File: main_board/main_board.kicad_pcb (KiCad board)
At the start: 2 copper layers, 20.3 x 15.2 mm, 18 parts, among them J1 Conn_01x03, J2 Conn_01x03, U1 STC15W201S-35x-SOP16, U2 AP130-15Y

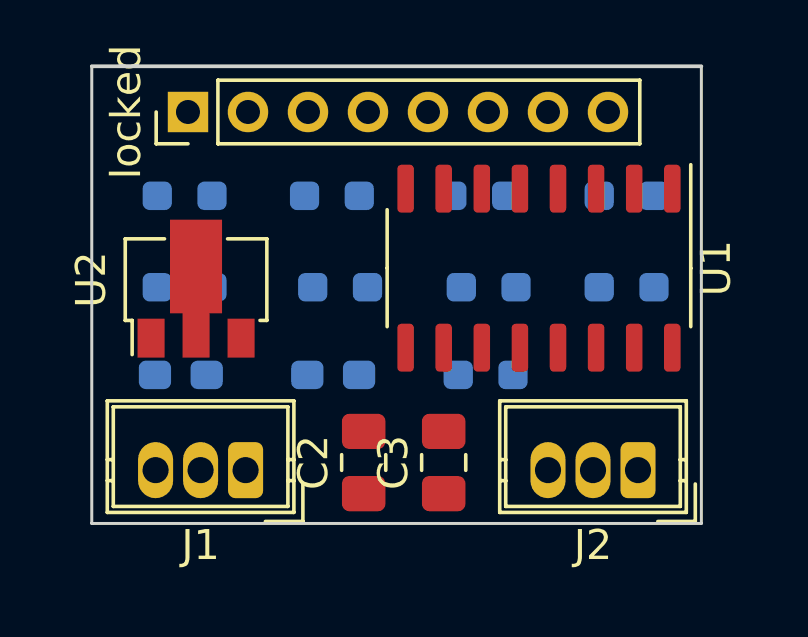
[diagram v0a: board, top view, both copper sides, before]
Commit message: feat(main_board): connect net
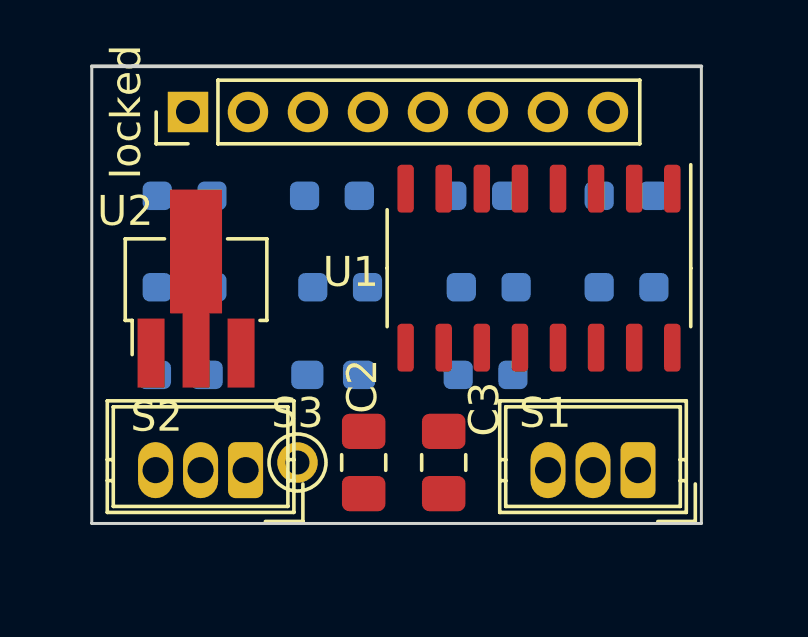
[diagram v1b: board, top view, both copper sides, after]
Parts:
- removed J1, J2: Conn_01x03, Connector_Wuerth:Wuerth_WR-WTB_64800311622_1x03_P1.50mm_Vertical
- added S1: Conn_01x03, Connector_Wuerth:Wuerth_WR-WTB_64800311622_1x03_P1.50mm_Vertical, F.Cu at (145.2, 89.7)
- added S2: Conn_01x03, Connector_Wuerth:Wuerth_WR-WTB_64800311622_1x03_P1.50mm_Vertical, F.Cu at (132.1, 89.7)
- added S3: Conn_01x01, TestPoint:TestPoint_THTPad_D1.5mm_Drill0.7mm, F.Cu at (133.9, 89.4)
- U2: value AP130-15Y -> AMS1117-5.0; footprint Package_TO_SOT_SMD:SOT-89-3 -> Package_TO_SOT_SMD:SOT-89-3_Handsoldering
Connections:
- C1 pad 1: (no net) -> +5V
- C1 pad 2: (no net) -> GND
- C2 pad 1: (no net) -> +5V
- C2 pad 2: (no net) -> GND
- C3 pad 1: (no net) -> /VCC
- C3 pad 2: (no net) -> GND
- C4 pad 1: (no net) -> /VCC
- C4 pad 2: (no net) -> GND
- R1 pad 1: (no net) -> /P1.4
- R1 pad 2: (no net) -> /HL
- R2 pad 1: (no net) -> /P3.2
- R2 pad 2: (no net) -> /R
- R3 pad 1: (no net) -> /P3.1
- R3 pad 2: (no net) -> /F
- R4 pad 1: (no net) -> /P3.0
- R4 pad 2: (no net) -> /TL
- R5 pad 1: (no net) -> /P3.6
- R5 pad 2: (no net) -> /TL
- R6 pad 1: (no net) -> /P1.5
- R6 pad 2: (no net) -> /HL
- R7 pad 1: (no net) -> /P1.3
- R7 pad 2: (no net) -> /RT
- R8 pad 1: (no net) -> /P1.2
- R8 pad 2: (no net) -> /LT
- R9 pad 1: (no net) -> /P3.6
- R9 pad 2: (no net) -> /FW
- U1 pad 1: (no net) -> /P1.2
- U1 pad 10: (no net) -> /P3.1
- U1 pad 11: (no net) -> /P3.2
- U1 pad 12: (no net) -> unconnected-(U1-INT1/P3.3-Pad12)
- U1 pad 13: (no net) -> /P3.6
- U1 pad 14: (no net) -> /P3.7
- U1 pad 15: (no net) -> /P1.0
- U1 pad 16: (no net) -> /P1.1
- U1 pad 2: (no net) -> /P1.3
- U1 pad 3: (no net) -> /P1.4
- U1 pad 4: (no net) -> /P1.5
- U1 pad 5: (no net) -> unconnected-(U1-CMP-/MCLKO/RST/P5.4-Pad5)
- U1 pad 6: (no net) -> /VCC
- U1 pad 7: (no net) -> unconnected-(U1-CMP+/P5.5-Pad7)
- U1 pad 8: (no net) -> GND
- U1 pad 9: (no net) -> /P3.0
- U2 pad 1: (no net) -> GND
- U2 pad 2: (no net) -> /VCC
- U2 pad 3: (no net) -> +5V
- locked pad 1: (no net) -> /VCC
- locked pad 2: (no net) -> /HL
- locked pad 3: (no net) -> /FW
- locked pad 4: (no net) -> /TL
- locked pad 5: (no net) -> /F
- locked pad 6: (no net) -> /R
- locked pad 7: (no net) -> /RT
- locked pad 8: (no net) -> /LT

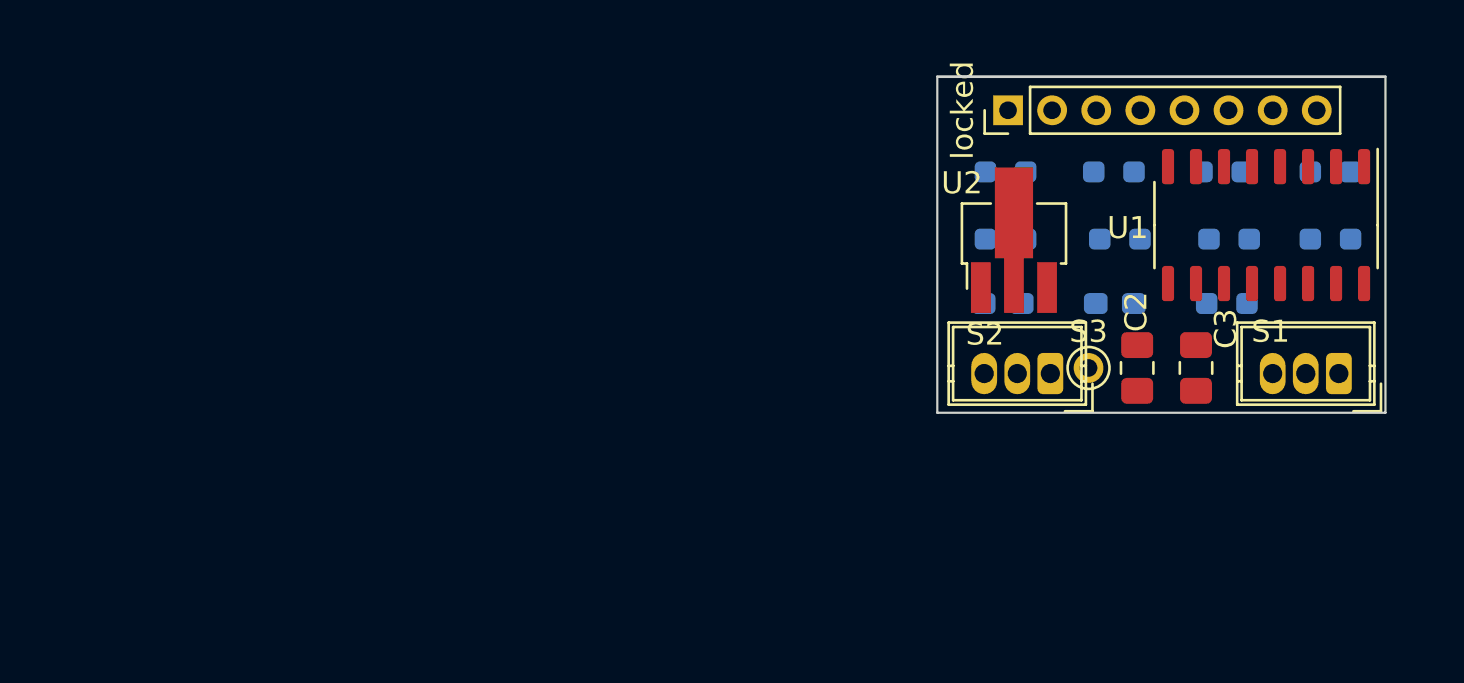
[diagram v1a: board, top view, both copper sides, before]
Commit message: feat(board/mcu): change mcu to sn32f805
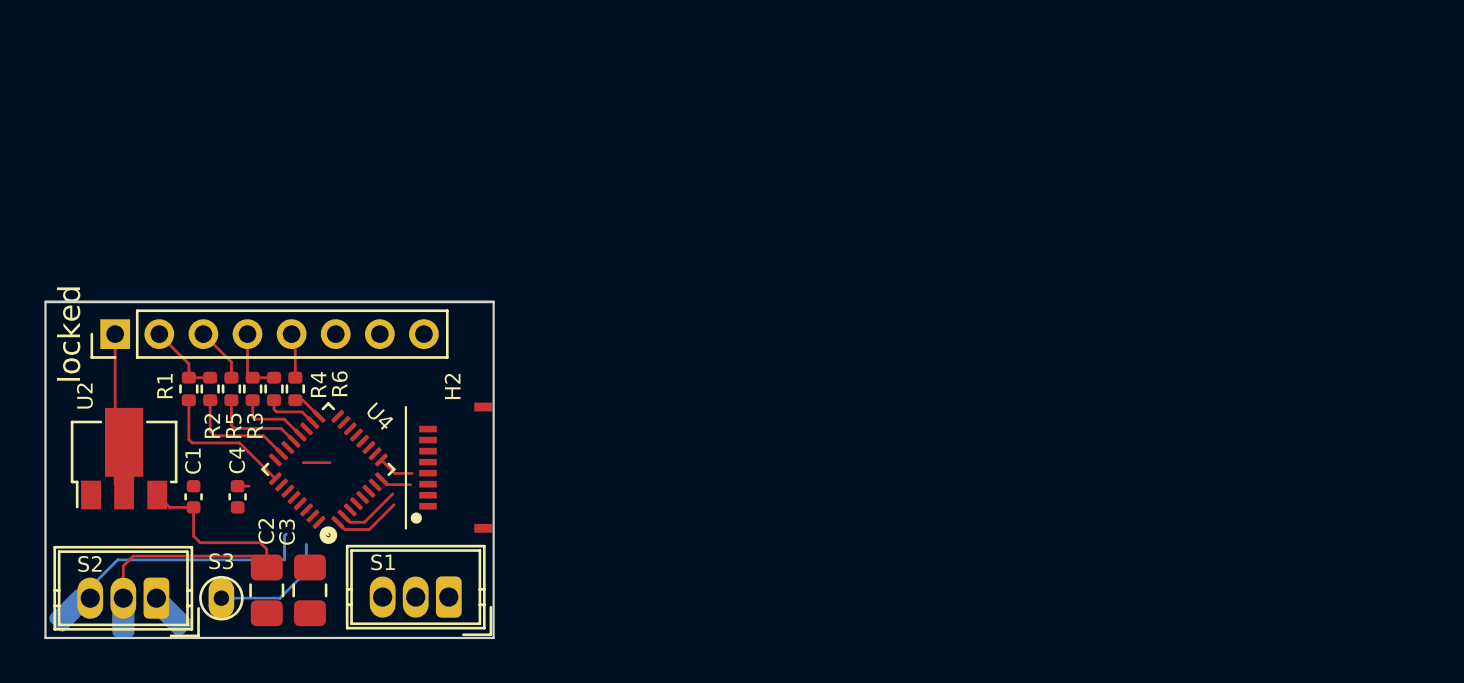
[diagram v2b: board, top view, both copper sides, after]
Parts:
- removed R7, R8, R9: R, Resistor_SMD:R_0603_1608Metric_Pad0.98x0.95mm_HandSolder
- removed U1: STC15W201S-35x-SOP16, Package_SO:STC_SOP-16_3.9x9.9mm_P1.27mm
- added H2: Conn_01x08, Connector_FFC-FPC:TE_0-1734839-8_1x08-1MP_P0.5mm_Horizontal, F.Cu at (104.8, 93.9)
- added REF**: SolderWirePad_1x01_SMD_1x2mm, Connector_Wire:SolderWirePad_1x01_SMD_1x2mm, B.Cu at (92.3, 100.6)
- added REF**: SolderWirePad_1x01_SMD_1x2mm, Connector_Wire:SolderWirePad_1x01_SMD_1x2mm, B.Cu at (87.7, 100.4)
- added REF**: SolderWirePad_1x01_SMD_1x2mm, Connector_Wire:SolderWirePad_1x01_SMD_1x2mm, B.Cu at (90.1, 100.6)
- added U4: SN32F805J/F, Package_DFN_QFN:QFN-32-1EP_4x4mm_P0.4mm_EP2.9x2.9mm, F.Cu at (99.4, 94.0)
- C1, C4: footprint Capacitor_SMD:C_0603_1608Metric_Pad1.08x0.95mm_HandSolder -> Capacitor_SMD:C_0402_1005Metric; moved to F.Cu
- R1, R2, R3, R4, R5, R6: footprint Resistor_SMD:R_0603_1608Metric_Pad0.98x0.95mm_HandSolder -> Resistor_SMD:R_0402_1005Metric; moved to F.Cu
- U2: footprint Package_TO_SOT_SMD:SOT-89-3_Handsoldering -> Package_TO_SOT_SMD:SOT-89-3
- moved R1 52.2 mm to (93.1, 90.4), turned to 90 degrees
- moved R6 42.9 mm to (97.9, 90.4), turned to 90 degrees
- moved R2 41.8 mm to (94.0, 90.4), turned to 90 degrees
- moved S2 41.8 mm to (91.6, 99.8)
- moved locked 41.7 mm to (89.7, 87.9)
- moved S1 41.6 mm to (104.9, 99.8)
- moved U2 41.5 mm to (90.1, 93.2)
- moved C3 41.4 mm to (98.6, 99.5), turned to -90 degrees
- moved C2 40.7 mm to (96.6, 99.5), turned to -90 degrees
- moved C4 40.7 mm to (95.3, 95.2), turned to -90 degrees
- moved S3 40.7 mm to (94.5, 99.8)
- moved R4 39.3 mm to (96.9, 90.4), turned to 90 degrees
- moved C1 37.7 mm to (93.3, 95.2), turned to 90 degrees
- moved R5 36.5 mm to (95.0, 90.4), turned to 90 degrees
- moved R3 34.8 mm to (96.0, 90.4), turned to 90 degrees
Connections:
- R1 pad 1: /P1.4 -> /HEAD_0
- R1 pad 2: /HL -> /LED_HEAD
- R2 pad 1: /P3.2 -> /HEAD_1
- R2 pad 2: /R -> /LED_HEAD
- R3 pad 1: /P3.1 -> /TAIL_0
- R3 pad 2: /F -> /LED_TAIL
- R4 pad 1: /P3.0 -> /TAIL_1
- R4 pad 2: /TL -> /LED_TAIL
- R5 pad 1: /P3.6 -> /CHASSIS
- R5 pad 2: /TL -> /LED_CHASSIS
- R6 pad 1: /P1.5 -> /FIRE
- R6 pad 2: /HL -> /LED_FIRE
- S3 pad 1: /P3.7 -> unconnected-(S3-Pin_1-Pad1)
- locked pad 2: /HL -> /LED_HEAD
- locked pad 3: /FW -> /LED_CHASSIS
- locked pad 4: /TL -> /LED_TAIL
- locked pad 5: /F -> /LED_FIRE
- locked pad 6: /R -> unconnected-(JSL1-Pin_6-Pad6)
- locked pad 7: /RT -> unconnected-(JSL1-Pin_7-Pad7)
- locked pad 8: /LT -> unconnected-(JSL1-Pin_8-Pad8)
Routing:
- net +5V: track 0.00 -> 15.9 mm
- net /P1.0: track 0.00 -> 11.0 mm
- net /VCC: track 0.00 -> 7.90 mm
- net /HEAD_0: track 0.00 -> 6.45 mm
- net unconnected-(S3-Pin_1-Pad1): track 0.00 -> 5.59 mm
- net /HEAD_1: track 0.00 -> 4.80 mm
- net /CHASSIS: track 0.00 -> 4.28 mm
- net /LED_HEAD: track 0.00 -> 3.49 mm
- net /SWDIO: track 0.00 -> 3.15 mm
- net /LED_TAIL: track 0.00 -> 3.04 mm
- net /TAIL_0: track 0.00 -> 2.92 mm
- net /SWCLK: track 0.00 -> 2.86 mm
- net /LED_CHASSIS: track 0.00 -> 2.50 mm
- net /TAIL_1: track 0.00 -> 2.42 mm
- net /LED_FIRE: track 0.00 -> 2.05 mm
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
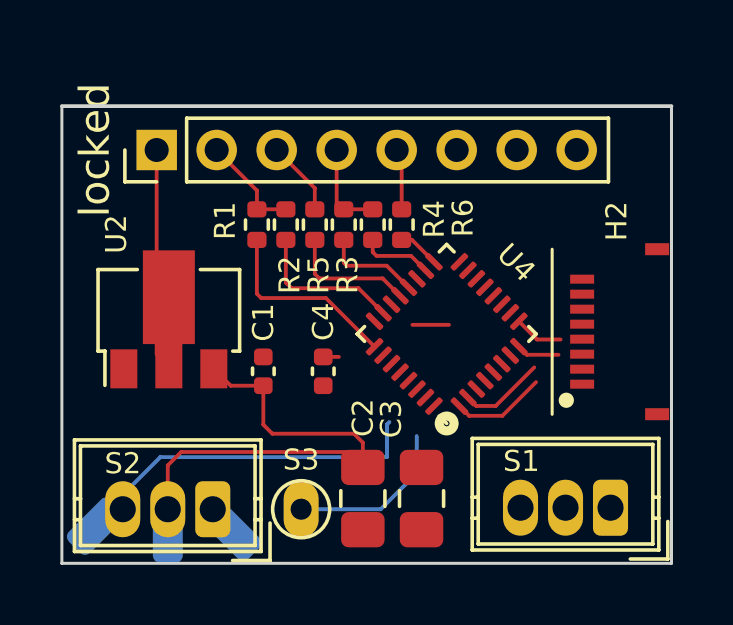
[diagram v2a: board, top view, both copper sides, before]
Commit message: feat(board/mcu): change mcu to STM32G031G8U8
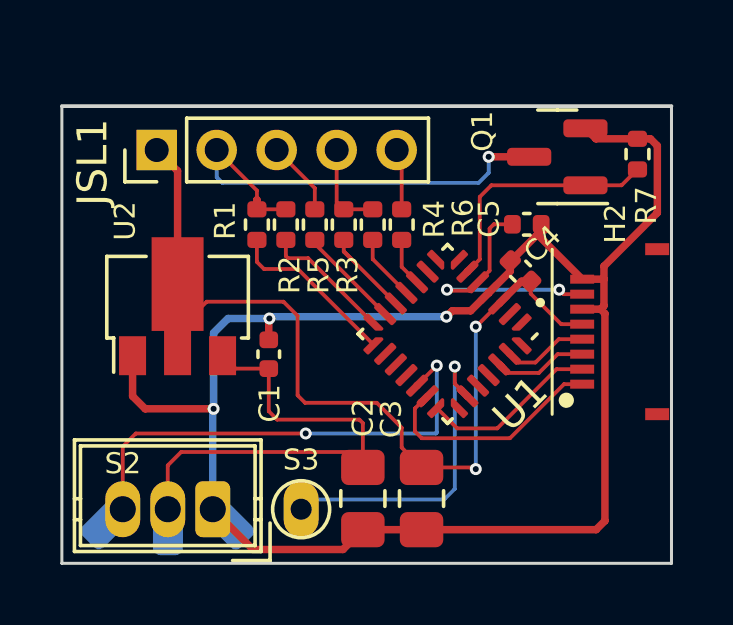
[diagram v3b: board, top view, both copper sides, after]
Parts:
- removed the REF** at (92.3, 100.6)
- removed the REF** at (87.7, 100.4)
- removed the REF** at (90.1, 100.6)
- removed S1: Conn_01x03, Connector_Wuerth:Wuerth_WR-WTB_64800311622_1x03_P1.50mm_Vertical
- removed U4: SN32F805J/F, Package_DFN_QFN:QFN-32-1EP_4x4mm_P0.4mm_EP2.9x2.9mm
- removed locked: Conn_01x08, Connector_PinHeader_2.00mm:PinHeader_1x08_P2.00mm_Vertical
- added C5: C, Capacitor_SMD:C_0402_1005Metric, F.Cu at (102.1, 90.3)
- added JSL1: Conn_01x05, Connector_PinHeader_2.00mm:PinHeader_1x05_P2.00mm_Vertical, F.Cu at (89.7, 87.9)
- added Q1: NMOS, Package_TO_SOT_SMD:SOT-23, F.Cu at (103.1, 88.1)
- added R7: R, Resistor_SMD:R_0402_1005Metric, F.Cu at (105.8, 88.0)
- added REF**: SolderWirePad_1x01_SMD_1x2mm, Connector_Wire:SolderWirePad_1x01_SMD_1x2mm, B.Cu at (88.2, 100.2)
- added REF**: SolderWirePad_1x01_SMD_1x2mm, Connector_Wire:SolderWirePad_1x01_SMD_1x2mm, B.Cu at (92.0, 100.2)
- added REF**: SolderWirePad_1x01_SMD_1x2mm, Connector_Wire:SolderWirePad_1x01_SMD_1x2mm, B.Cu at (90.1, 100.4)
- added U1: STM32G031G8Ux, Package_DFN_QFN:QFN-28_4x4mm_P0.5mm, F.Cu at (99.4, 94.0)
- moved C4 7.37 mm to (101.8, 91.9), turned to 135 degrees
- moved C1 0.60 mm to (93.5, 94.7)
- moved U2 0.53 mm to (90.4, 92.8)
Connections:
- H2 pad 1: unconnected-(H2-Pin_1-Pad1) -> /SWDIO
- H2 pad 2: unconnected-(H2-Pin_2-Pad2) -> /SWCLK
- H2 pad 3: unconnected-(H2-Pin_3-Pad3) -> /UART_TX
- H2 pad 4: unconnected-(H2-Pin_4-Pad4) -> /UART_RX
- H2 pad 5: unconnected-(H2-Pin_5-Pad5) -> /VCC
- H2 pad 6: unconnected-(H2-Pin_6-Pad6) -> GND
- H2 pad 7: unconnected-(H2-Pin_7-Pad7) -> /RST
- H2 pad 8: unconnected-(H2-Pin_8-Pad8) -> GND
- S2 pad 3: /P1.0 -> /SG_THRO
- S3 pad 1: unconnected-(S3-Pin_1-Pad1) -> /SG_BT
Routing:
- net GND: track 1.23 -> 57.0 mm, vias 0 -> 3
- net /VCC: track 7.90 -> 32.1 mm, vias 0 -> 2
- net /SG_THRO: track 0.00 -> 15.9 mm, vias 0 -> 2
- net /LED_HEAD: track 3.49 -> 15.9 mm, vias 0 -> 1
- net /P1.0: track 11.0 -> 0.00 mm
- net /SG_BT: track 0.00 -> 10.9 mm, vias 0 -> 1
- net /SW: track 0.00 -> 8.59 mm
- net /RST: track 0.00 -> 8.50 mm, vias 0 -> 2
- net unconnected-(S3-Pin_1-Pad1): track 5.59 -> 0.00 mm
- net /SWDIO: track 3.15 -> 8.06 mm
- net /SWCLK: track 2.86 -> 5.94 mm
- net /UART_TX: track 1.65 -> 3.43 mm
- net /UART_RX: track 1.44 -> 2.85 mm
- net /CHASSIS: track 4.28 -> 3.44 mm
- net /HEAD_0: track 6.45 -> 5.76 mm

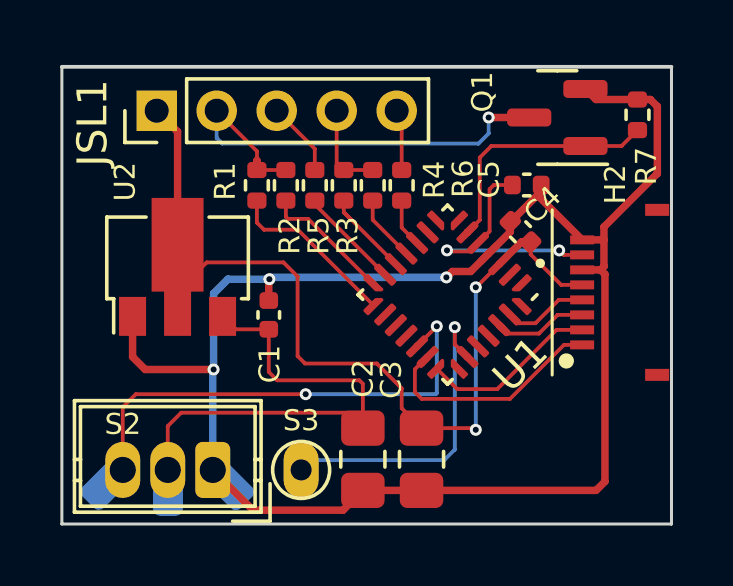
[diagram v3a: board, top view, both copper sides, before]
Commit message: feat(board): update ohm
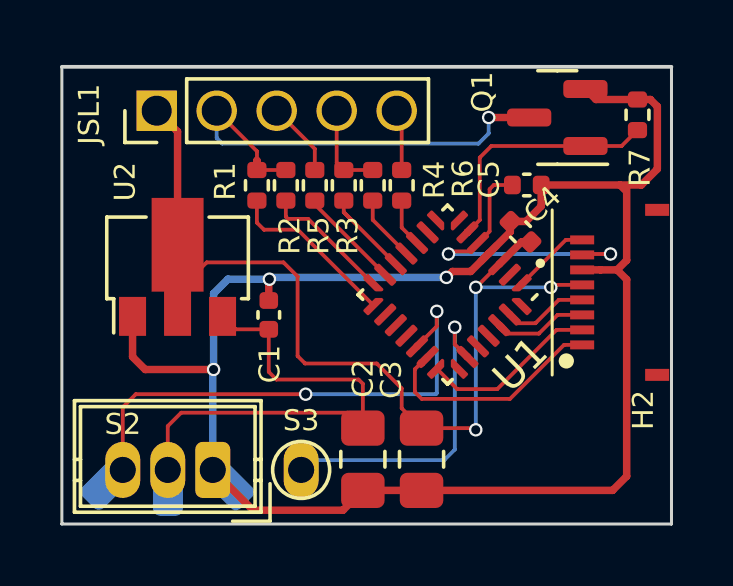
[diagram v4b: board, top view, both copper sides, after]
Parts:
- C1, C4, C5: value C -> 100n
- C2, C3: value C -> 10u
- R1, R2, R3, R4, R5, R6, R7: value R -> 100
- U2: value AMS1117-5.0 -> AMS1117-3.3
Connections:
- H2 pad 8: GND -> /TP1
- U1 pad 1: unconnected-(U1-PC14-Pad1) -> /TP1
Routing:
- net /TP1: track 0.00 -> 2.63 mm
- net /RST: track 8.50 -> 10.4 mm
- net GND: track 57.0 -> 58.7 mm
- net /VCC: track 32.1 -> 33.2 mm, vias 2 -> 3
- net /SG_THRO: track 15.9 -> 16.9 mm

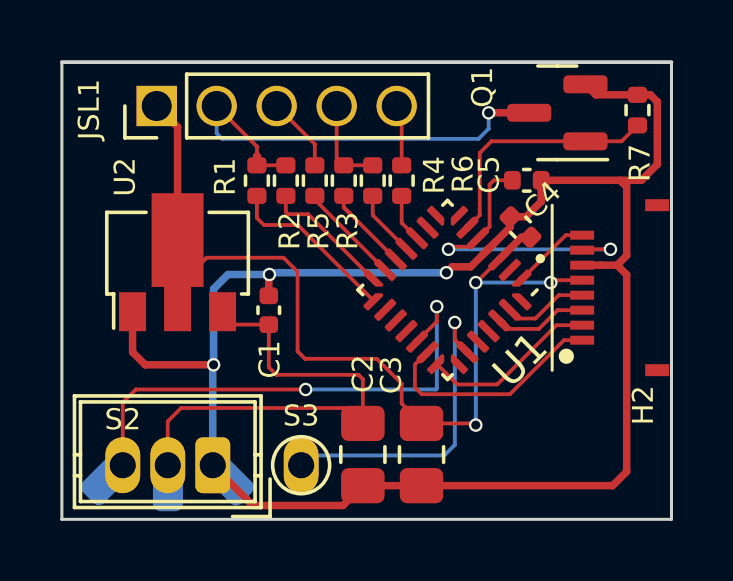
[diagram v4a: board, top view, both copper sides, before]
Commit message: feat(main_board): modify placement
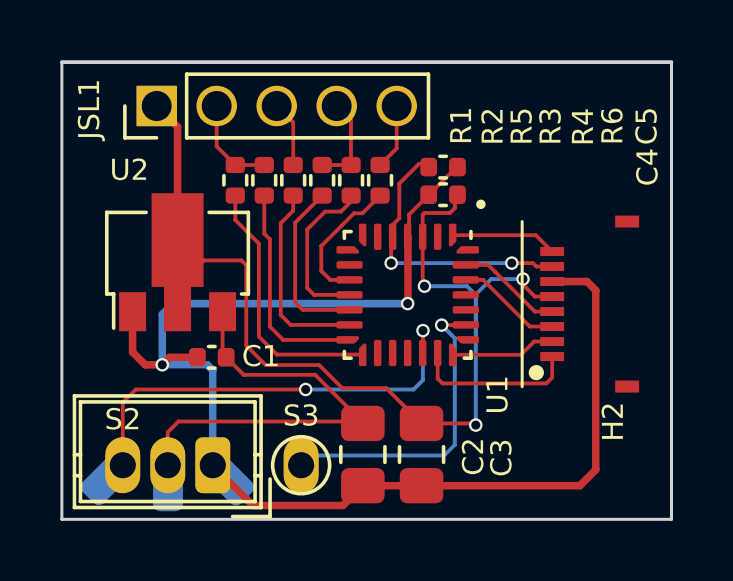
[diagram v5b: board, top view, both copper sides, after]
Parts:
- removed Q1: NMOS, Package_TO_SOT_SMD:SOT-23
- removed R7: 100, Resistor_SMD:R_0402_1005Metric
- moved C5 2.82 mm to (99.3, 89.9)
- moved C4 2.80 mm to (99.3, 90.8), turned to 180 degrees
- moved C1 2.46 mm to (91.6, 96.2), turned to 180 degrees
- moved U1 1.34 mm to (98.1, 94.2), turned to -90 degrees
- moved H2 1.14 mm to (103.8, 94.5)
- moved R1 0.72 mm to (92.3, 90.3)
- moved R2 0.72 mm to (93.3, 90.3)
- moved R3 0.72 mm to (95.2, 90.3)
- moved R4 0.72 mm to (96.2, 90.3)
- moved R5 0.72 mm to (94.3, 90.3)
- moved R6 0.72 mm to (97.2, 90.3)
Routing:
- net GND: track 58.7 -> 45.0 mm, vias 3 -> 2
- net /LED_HEAD: track 15.9 -> 3.19 mm, vias 1 -> 0
- net /SW: track 8.59 -> 0.00 mm
- net /VCC: track 33.2 -> 36.8 mm
- net /TAIL_1: track 2.23 -> 5.51 mm
- net /CHASSIS: track 3.44 -> 6.58 mm
- net /HEAD_0: track 5.76 -> 8.74 mm
- net /FIRE: track 1.62 -> 4.55 mm
- net /HEAD_1: track 4.39 -> 7.22 mm
- net /TAIL_0: track 3.21 -> 5.89 mm
- net /SWDIO: track 8.06 -> 5.51 mm
- net /SWCLK: track 5.94 -> 3.50 mm
- net /SG_THRO: track 16.9 -> 14.8 mm
- net +5V: track 16.3 -> 14.7 mm
- net /RST: track 10.4 -> 9.34 mm
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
